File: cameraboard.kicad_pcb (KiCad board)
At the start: 2 copper layers, 46.8 x 46.8 mm, 14 parts, among them J1 02x10 1.27mm, J2 Micro_SD_Card, J3 Conn 01x10 1.27mm, Q1 Nikla_Vision, Q2 SSM3J133TU,LF

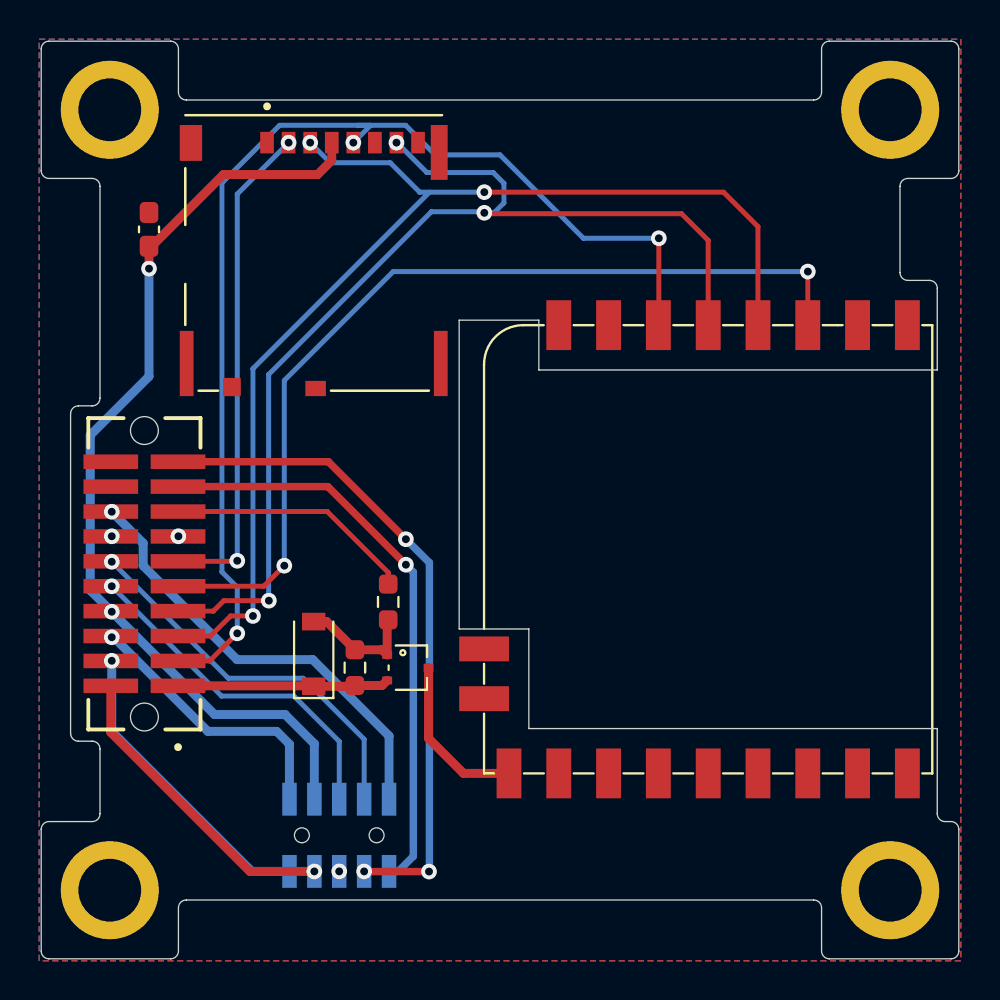
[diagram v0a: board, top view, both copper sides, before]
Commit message: Moved connectors as recommended
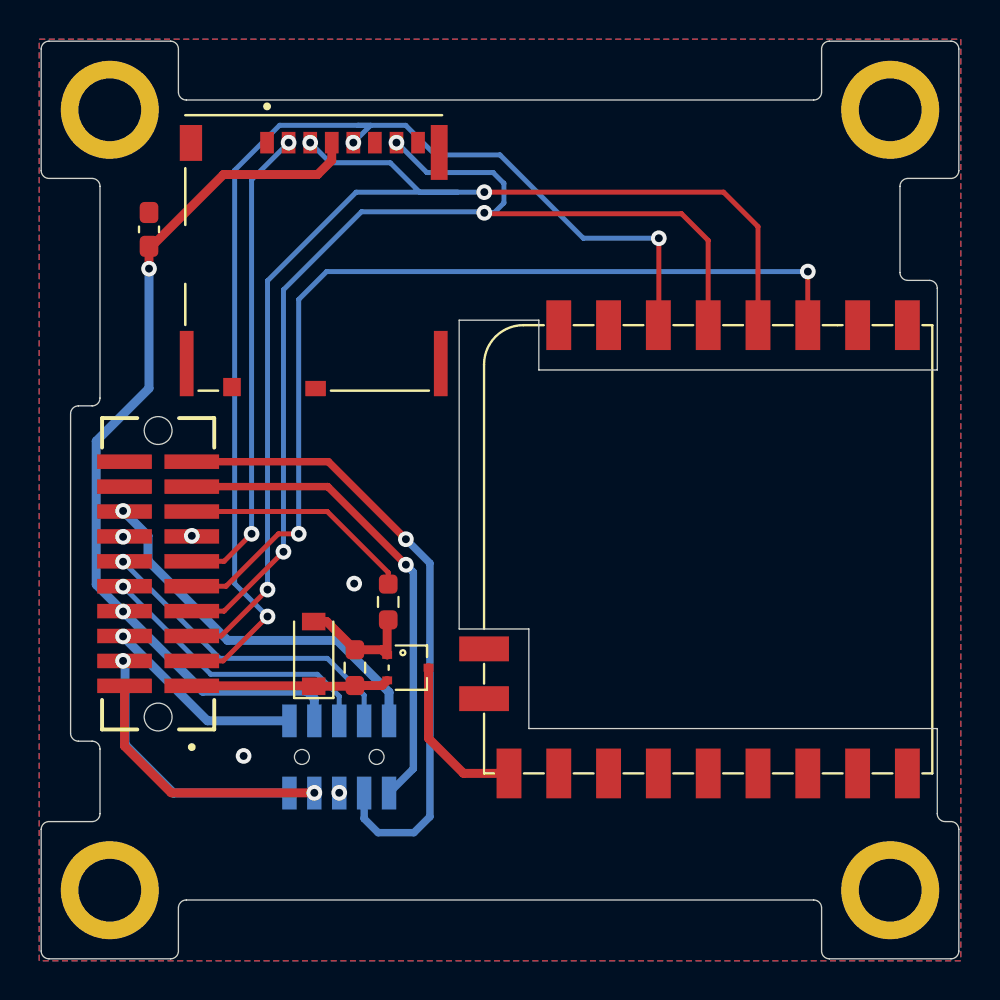
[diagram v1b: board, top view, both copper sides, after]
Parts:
- moved J3 4.00 mm to (98.5, 73.3)
- moved J1 0.70 mm to (89.3, 64.0)
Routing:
- net COIL6_N: track 29.9 -> 24.9 mm
- net BATT_P_SW: track 14.1 -> 10.3 mm
- net SDA3: track 19.7 -> 16.4 mm
- net +3V3: track 48.0 -> 44.8 mm
- net SCL3: track 17.8 -> 14.6 mm
- net VBUS: track 22.8 -> 19.6 mm
- net /MOSI: track 59.2 -> 61.8 mm
- net BATT_P: track 15.7 -> 13.7 mm
- net BATT_N_SW: track 15.6 -> 13.7 mm
- net COIL6_P: track 34.0 -> 32.5 mm, vias 3 -> 1
- net /SD_CS: track 25.4 -> 24.4 mm
- net /CAM_CS: track 47.0 -> 47.8 mm
- net /CAM_EN: track 12.6 -> 11.9 mm
- net GND: vias 3 -> 5

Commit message: Rename VBUS to VUSB and export files
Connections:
- net VBUS renamed VUSB
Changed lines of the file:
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@@
   (net 28 "SCL3")
   (net 29 "SDA3")
-  (net 30 "VBUS")
+  (net 30 "VUSB")
   (net 31 "COIL6_N")
   (net 32 "COIL6_P")
@@
       (net 21 "/CAM_EN") (pinfunction "Pin_15") (pintype "passive"))
     (pad "16" smd rect (at 3.175 -1.715 90) (size 0.74 2.79) (layers "F.Cu" "F.Paste" "F.Mask")
-      (net 30 "VBUS") (pinfunction "Pin_16") (pintype "passive"))
+      (net 30 "VUSB") (pinfunction "Pin_16") (pintype "passive"))
     (pad "17" smd rect (at 4.445 1.715 90) (size 0.74 2.79) (layers "F.Cu" "F.Paste" "F.Mask")
       (net 31 "COIL6_N") (pinfunction "Pin_17") (pintype "passive"))
@@
       (net 31 "COIL6_N") (pinfunction "Pin_9") (pintype "passive"))
     (pad "10" smd rect (at 2.54 -1.8425) (size 0.74 1.675) (layers "B.Cu" "B.Paste" "B.Mask")
-      (net 30 "VBUS") (pinfunction "Pin_10") (pintype "passive"))
+      (net 30 "VUSB") (pinfunction "Pin_10") (pintype "passive"))
     (model "${KIPRJMOD}/kicad-libs/3d/FLE-105-01-G-DV-A.step" hide
       (offset (xyz 0 0 0.1524))

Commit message: Added Logo, version number and date
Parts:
- Ref**: moved to B.Cu
- moved Ref** 21.4 mm to (102.0, 55.5), turned to 90 degrees
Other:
- board text added: "v02 09-JUN-22"
- board text removed: "v02"
